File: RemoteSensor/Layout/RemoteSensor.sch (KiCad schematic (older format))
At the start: 47 parts, among them J1 PRG_HEADER, J2 LCD_HEADER, J3 USB_B_Micro, J4 BATT_CONN, Q1 2N7002, Q2 2N7002, Q3 2N7002, SW1 BTN_RST, SW2 BTN_LOAD, SW3 SW_DPDT_x2, U1 ESP-12F, U2 74LVC2G02, U3 LM50CIM3, U4 MCP73831-2-OT, U5 LM3670MF, U6 BD48ExxG, U7 BD48ExxG

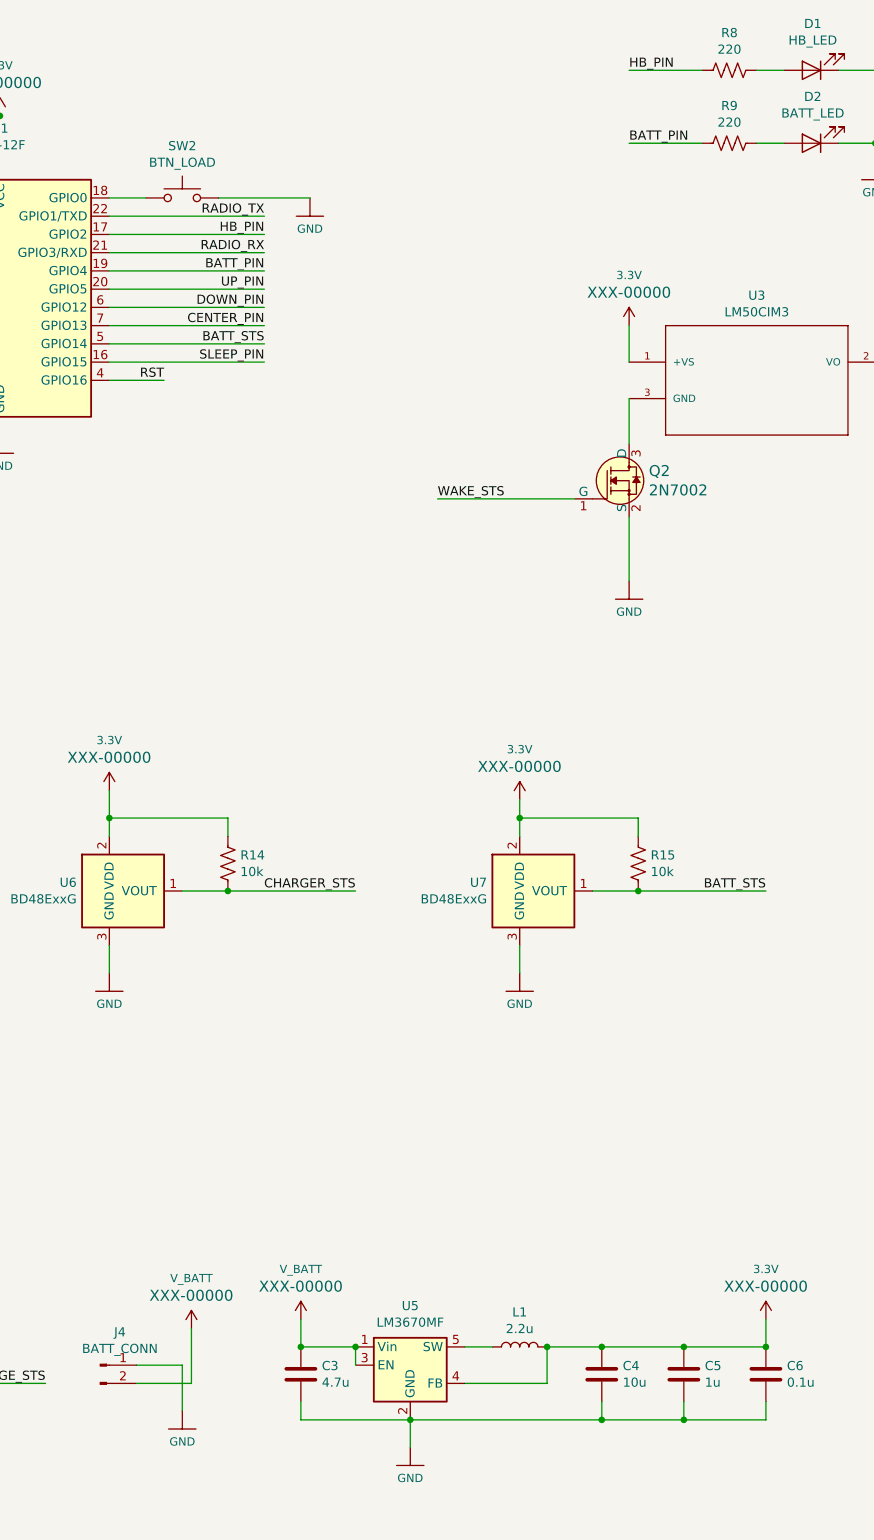
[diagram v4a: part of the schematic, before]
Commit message: Change some component values
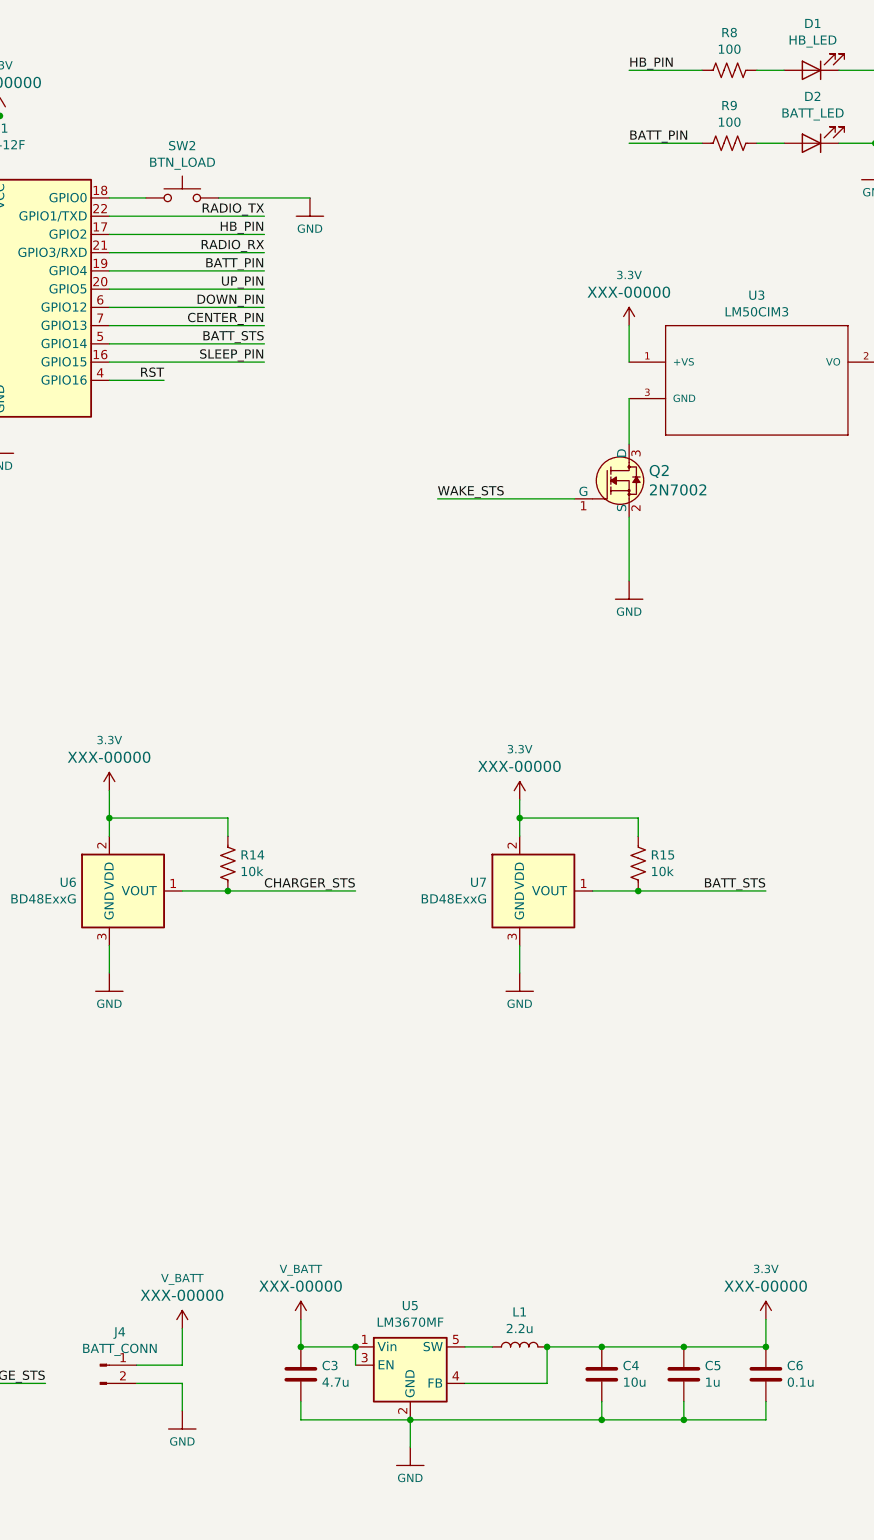
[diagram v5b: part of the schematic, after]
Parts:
- R8, R9: value 220 -> 100
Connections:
- net GND: now also J4.2 (Pin_2); no longer J4.1 (Pin_1)
- net V_BATT: now also J4.1 (Pin_1); no longer J4.2 (Pin_2)
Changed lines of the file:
@@
 P 9050 1100
 F 0 "R8" V 9255 1100 50  0000 C CNN
-F 1 "220" V 9164 1100 50  0000 C CNN
+F 1 "100" V 9164 1100 50  0000 C CNN
 F 2 "Resistor_SMD:R_0603_1608Metric_Pad1.05x0.95mm_HandSolder" V 9090 1090 50  0001 C CNN
 F 3 "~" H 9050 1100 50  0001 C CNN
@@
 P 9050 1500
 F 0 "R9" V 8845 1500 50  0000 C CNN
-F 1 "220" V 8936 1500 50  0000 C CNN
+F 1 "100" V 8936 1500 50  0000 C CNN
 F 2 "Resistor_SMD:R_0603_1608Metric_Pad1.05x0.95mm_HandSolder" V 9090 1490 50  0001 C CNN
 F 3 "~" H 9050 1500 50  0001 C CNN
@@
 	1    0    0    -1
 $EndComp
-$Comp
-L SparkFun-PowerSymbols:V_BATT #SUPPLY0114
-U 1 1 5ED399F5
-P 6100 8000
-F 0 "#SUPPLY0114" H 6150 8000 45  0001 L BNN
-F 1 "V_BATT" H 6100 8276 45  0000 C CNN
-F 2 "XXX-00000" H 6100 8181 60  0000 C CNN
-F 3 "" H 6100 8000 60  0001 C CNN
-	1    6100 8000
-	1    0    0    -1
-$EndComp
 Wire Wire Line
 	7450 3450 8200 3450
@@
 Wire Wire Line
 	1250 8650 1350 8650
-Wire Wire Line
-	5800 8300 6100 8300
-Wire Wire Line
-	6100 8300 6100 8000
+$Comp
+L SparkFun-PowerSymbols:V_BATT #SUPPLY0114
+U 1 1 5ED399F5
+P 6050 8000
+F 0 "#SUPPLY0114" H 6100 8000 45  0001 L BNN
+F 1 "V_BATT" H 6050 8276 45  0000 C CNN
+F 2 "XXX-00000" H 6050 8181 60  0000 C CNN
+F 3 "" H 6050 8000 60  0001 C CNN
+	1    6050 8000
+	1    0    0    -1
+$EndComp
 Wire Wire Line
 	5800 8200 6050 8200
 Wire Wire Line
-	6050 8200 6050 8450
+	6050 8200 6050 8000
+Wire Wire Line
+	5800 8300 6050 8300
+Wire Wire Line
+	6050 8300 6050 8450
 $EndSCHEMATC

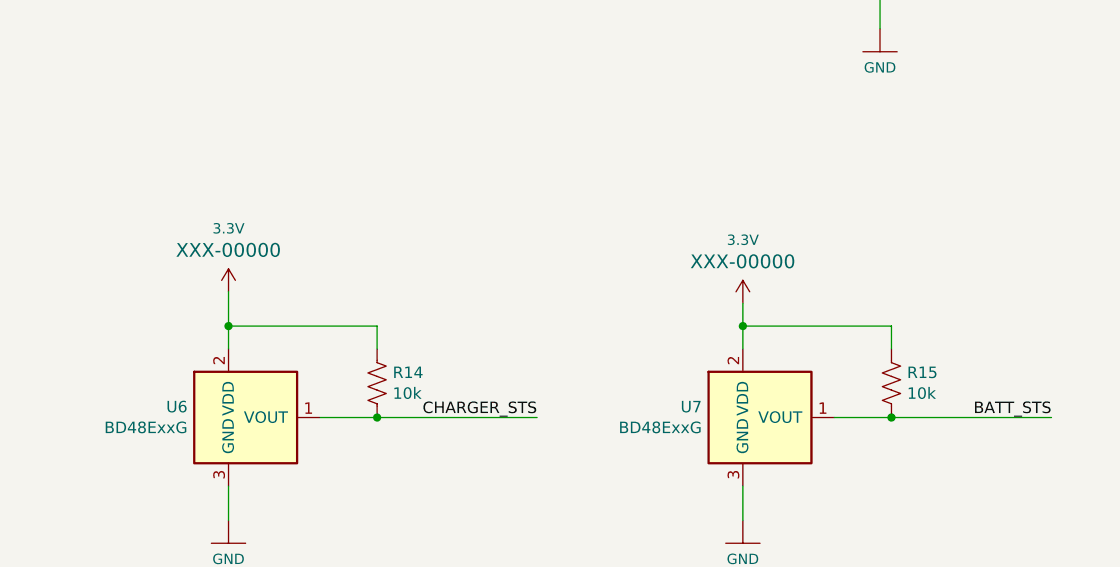
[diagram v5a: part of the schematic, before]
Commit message: Fix charger and battery status
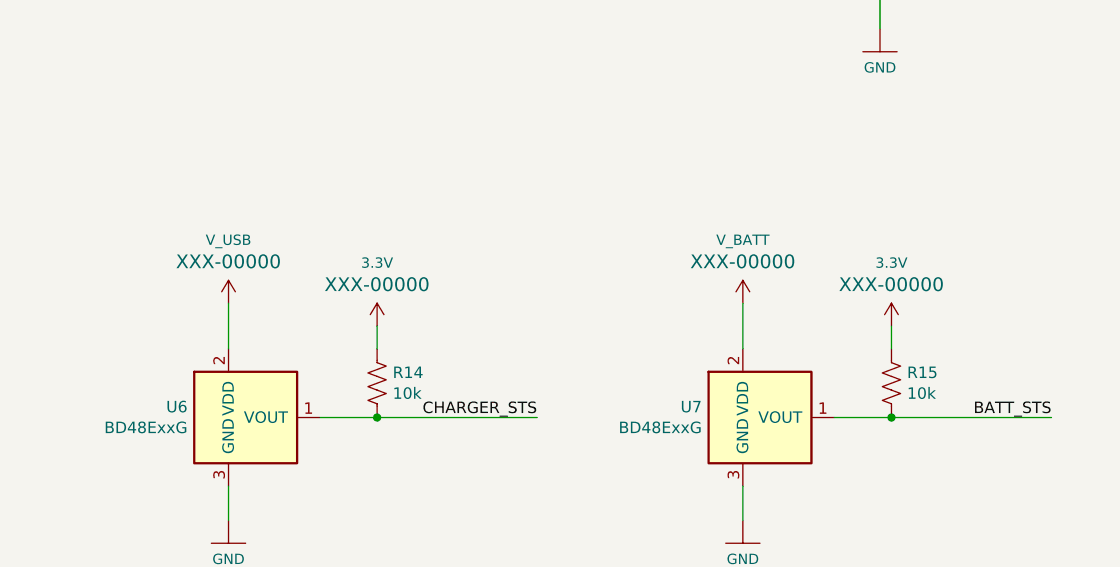
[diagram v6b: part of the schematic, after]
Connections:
- net 3.3V: no longer U6.2 (VDD), U7.2 (VDD)
- net V_BATT: now also U7.2 (VDD)
- net V_USB: now also U6.2 (VDD)
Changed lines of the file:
@@
 $EndComp
-Wire Wire Line
-	7900 5200 8550 5200
 Wire Wire Line
 	8550 5200 8550 5300
-Wire Wire Line
-	7900 5200 7900 5300
 Wire Wire Line
 	8550 5600 8300 5600
@@
 $EndComp
 Wire Wire Line
-	5650 5200 6300 5200
-Wire Wire Line
 	6300 5200 6300 5300
-Wire Wire Line
-	5650 5200 5650 5300
 Wire Wire Line
 	6300 5600 6050 5600
@@
 L SparkFun-PowerSymbols:3.3V #SUPPLY0112
 U 1 1 5EC8248B
-P 5650 5050
-F 0 "#SUPPLY0112" H 5700 5050 45  0001 L BNN
-F 1 "3.3V" H 5650 5326 45  0000 C CNN
-F 2 "XXX-00000" H 5650 5231 60  0000 C CNN
-F 3 "" H 5650 5050 60  0001 C CNN
-	1    5650 5050
+P 6300 5200
+F 0 "#SUPPLY0112" H 6350 5200 45  0001 L BNN
+F 1 "3.3V" H 6300 5476 45  0000 C CNN
+F 2 "XXX-00000" H 6300 5381 60  0000 C CNN
+F 3 "" H 6300 5200 60  0001 C CNN
+	1    6300 5200
 	1    0    0    -1
 $EndComp
@@
 L SparkFun-PowerSymbols:3.3V #SUPPLY0113
 U 1 1 5EC82E3D
-P 7900 5100
-F 0 "#SUPPLY0113" H 7950 5100 45  0001 L BNN
-F 1 "3.3V" H 7900 5376 45  0000 C CNN
-F 2 "XXX-00000" H 7900 5281 60  0000 C CNN
-F 3 "" H 7900 5100 60  0001 C CNN
-	1    7900 5100
-	1    0    0    -1
-$EndComp
-Wire Wire Line
-	7900 5100 7900 5200
-Connection ~ 7900 5200
-Wire Wire Line
-	5650 5050 5650 5200
-Connection ~ 5650 5200
+P 8550 5200
+F 0 "#SUPPLY0113" H 8600 5200 45  0001 L BNN
+F 1 "3.3V" H 8550 5476 45  0000 C CNN
+F 2 "XXX-00000" H 8550 5381 60  0000 C CNN
+F 3 "" H 8550 5200 60  0001 C CNN
+	1    8550 5200
+	1    0    0    -1
+$EndComp
 $Comp
 L dk_Transistors-FETs-MOSFETs-Single:2N7002 Q3
@@
 Wire Wire Line
 	6050 8300 6050 8450
+$Comp
+L SparkFun-PowerSymbols:V_USB #SUPPLY?
+U 1 1 5EE47119
+P 5650 5100
+F 0 "#SUPPLY?" H 5700 5100 45  0001 L BNN
+F 1 "V_USB" H 5650 5376 45  0000 C CNN
+F 2 "XXX-00000" H 5650 5281 60  0000 C CNN
+F 3 "" H 5650 5100 60  0001 C CNN
+	1    5650 5100
+	1    0    0    -1
+$EndComp
+$Comp
+L SparkFun-PowerSymbols:V_BATT #SUPPLY?
+U 1 1 5EE47A68
+P 7900 5100
+F 0 "#SUPPLY?" H 7950 5100 45  0001 L BNN
+F 1 "V_BATT" H 7900 5376 45  0000 C CNN
+F 2 "XXX-00000" H 7900 5281 60  0000 C CNN
+F 3 "" H 7900 5100 60  0001 C CNN
+	1    7900 5100
+	1    0    0    -1
+$EndComp
+Wire Wire Line
+	7900 5100 7900 5300
+Wire Wire Line
+	5650 5100 5650 5300
 $EndSCHEMATC

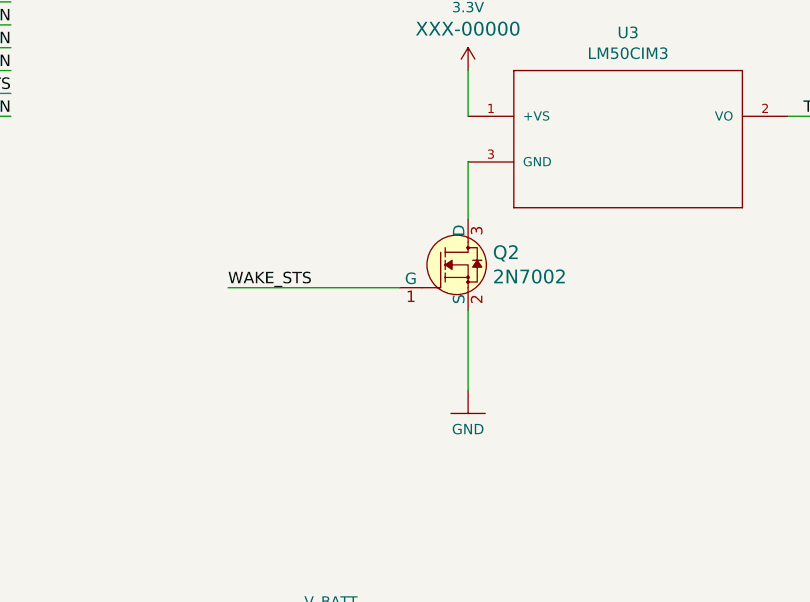
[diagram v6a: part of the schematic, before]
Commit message: Remove power control for temperature sensor
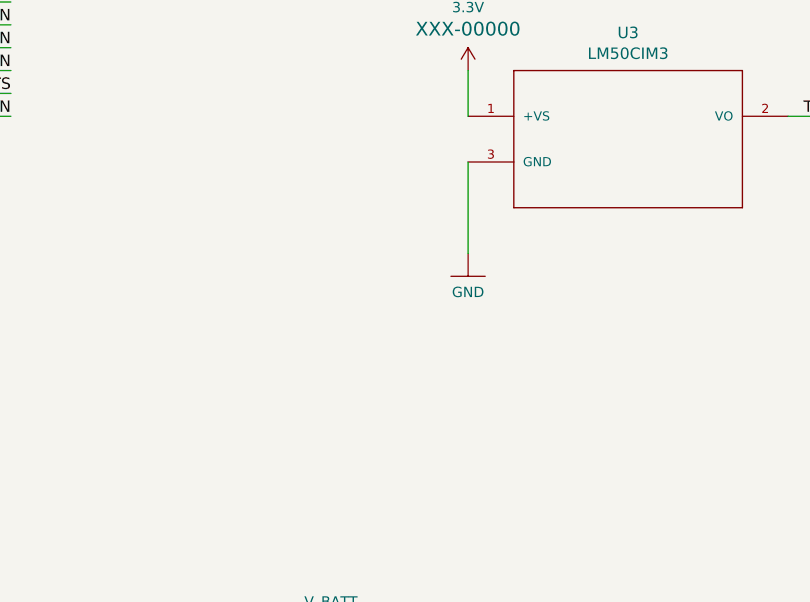
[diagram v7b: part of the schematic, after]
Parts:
- removed Q2: 2N7002, digikey-footprints:SOT-23-3, symbol dk_Transistors-FETs-MOSFETs-Single:2N7002
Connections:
- net GND: now also U3.3 (GND)

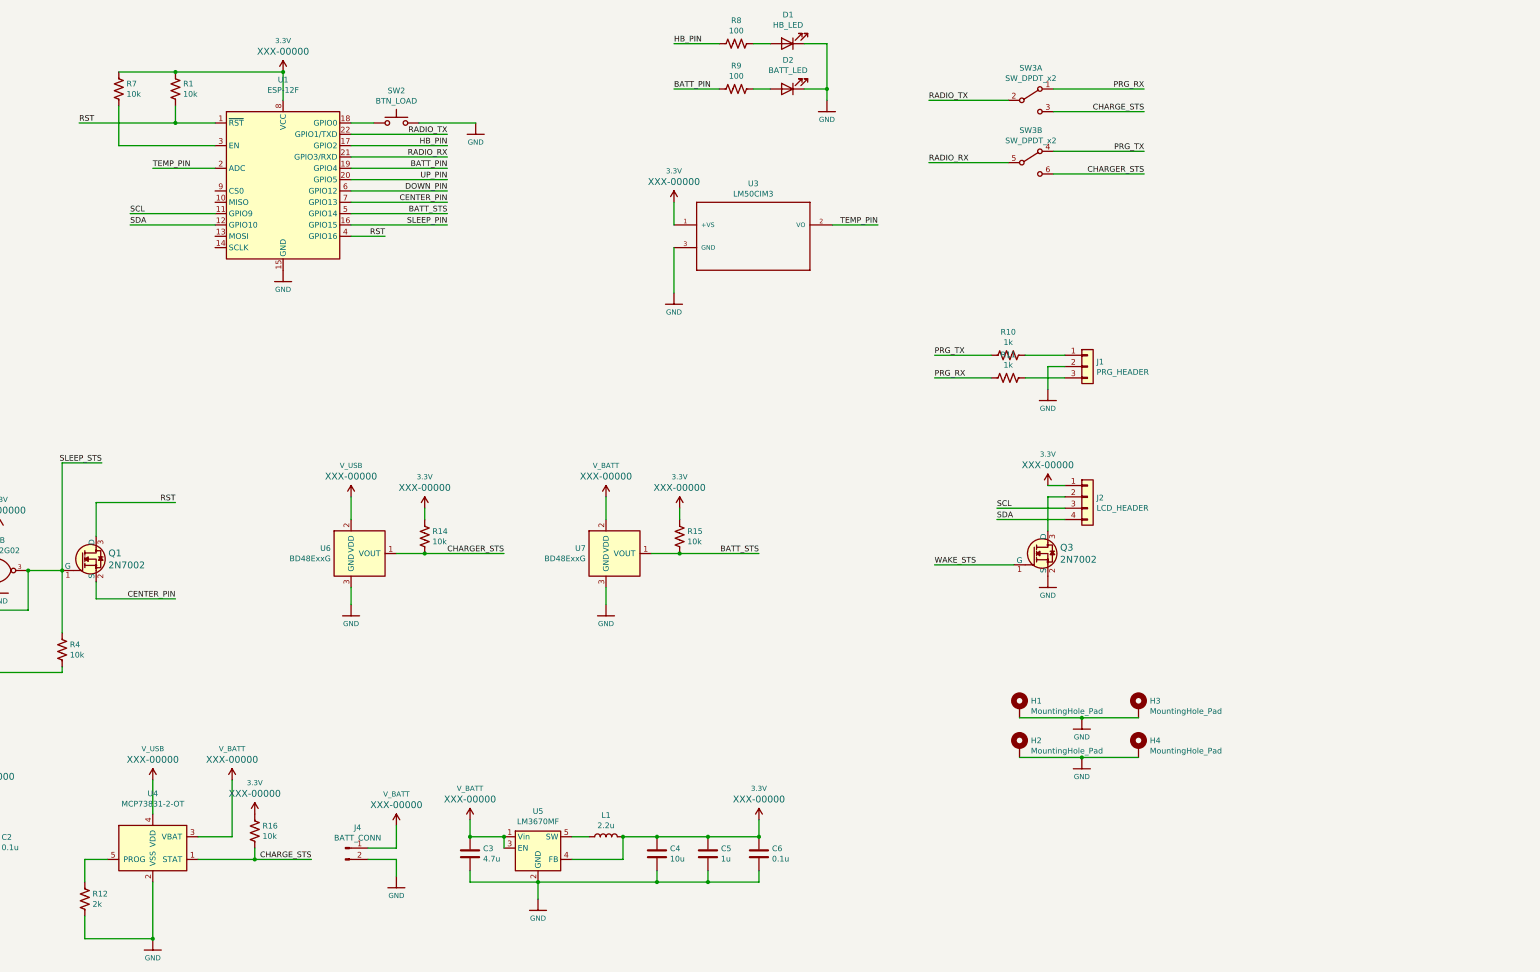
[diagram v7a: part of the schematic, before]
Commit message: Add second regulator for USB
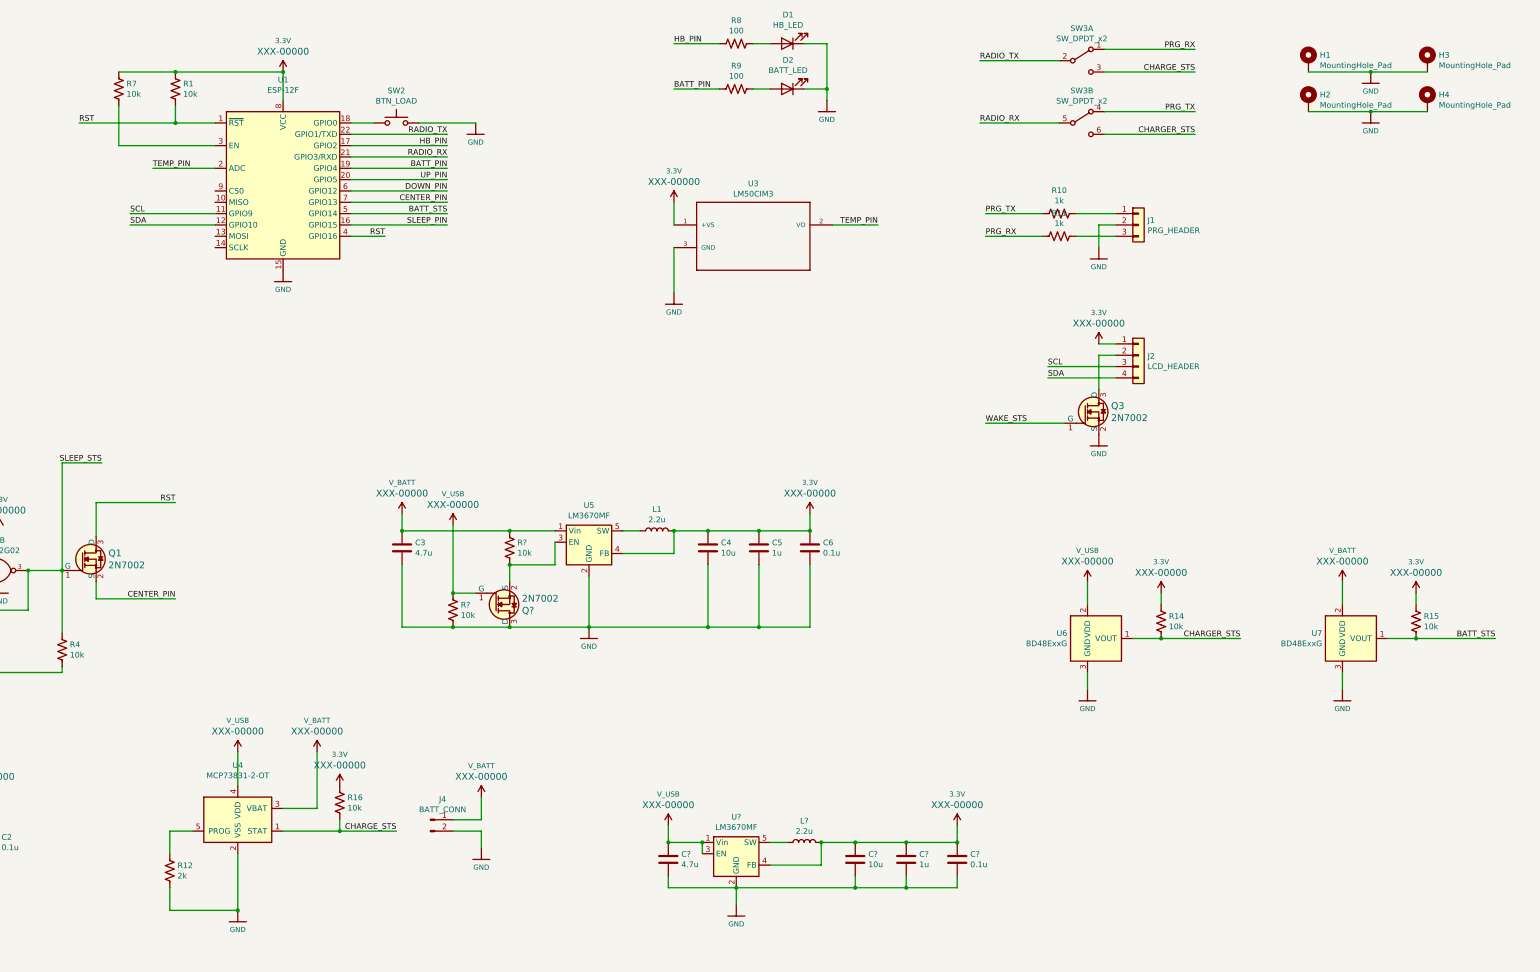
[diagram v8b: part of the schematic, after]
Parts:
- added C?: 4.7u, Capacitor_SMD:C_0603_1608Metric_Pad1.05x0.95mm_HandSolder, symbol Device:C
- added C?: 10u, Capacitor_SMD:C_0603_1608Metric_Pad1.05x0.95mm_HandSolder, symbol Device:C
- added C?: 1u, Capacitor_SMD:C_0603_1608Metric_Pad1.05x0.95mm_HandSolder, symbol Device:C
- added C?: 0.1u, Capacitor_SMD:C_0603_1608Metric_Pad1.05x0.95mm_HandSolder, symbol Device:C
- added L?: 2.2u, Inductor_SMD:L_0603_1608Metric_Pad1.05x0.95mm_HandSolder, symbol Device:L
- added Q?: 2N7002, digikey-footprints:SOT-23-3, symbol dk_Transistors-FETs-MOSFETs-Single:2N7002
- added R? (x2): 10k, symbol Device:R_US
- added U?: LM3670MF, Package_TO_SOT_SMD:TSOT-23-5, symbol Regulator_Switching:LM3670MF
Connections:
- net 3.3V: now also C?.1, C?.1, C?.1, L?.2, U?.4 (FB)
- net GND: now also C?.2, C?.2, C?.2, C?.2, Q?.3 (D), R?.2, U?.2 (GND)
- net V_BATT: now also R?.1; no longer U5.3 (EN)
- net V_USB: now also C?.1, Q?.1 (G), R?.1, U?.1 (Vin), U?.3 (EN)
- new net: Q?.2 (S), R?.2, U5.3 (EN)
- new net: L?.1, U?.5 (SW)
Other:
- moved on the sheet: C3, C4, C5, C6, H1, H2, H3, H4, J1, J2, J4, L1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
